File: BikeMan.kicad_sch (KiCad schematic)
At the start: 18 parts, among them J1 USB_A_stacked, J11 ExpansionSlotA, J12 ExpansionSlotB, J13 ExpansionSlotC, J14 CAN_{OUT}, J2 USB_A_stacked, J3 CAN_{IN}, J4 Barrel_Jack, J5 GPIO Outputs, J6 GPIO Inputs, J7 CAN / Power / GND

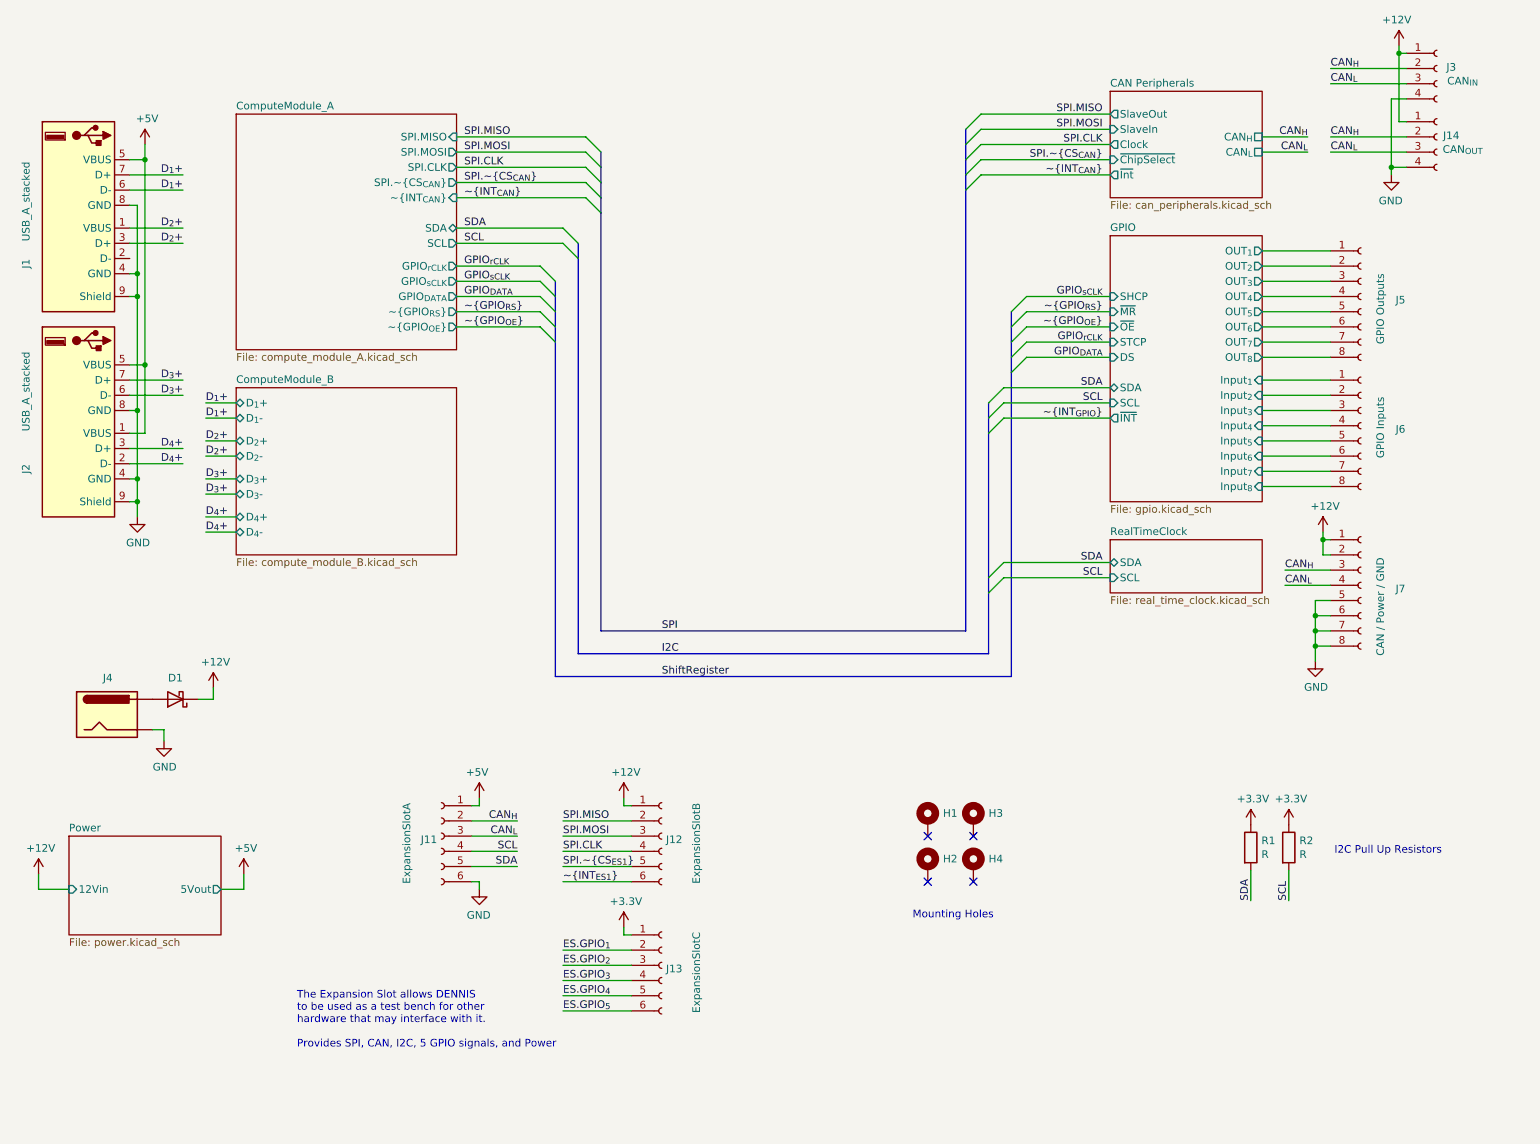
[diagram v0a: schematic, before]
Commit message: more layout: power supply and gpio
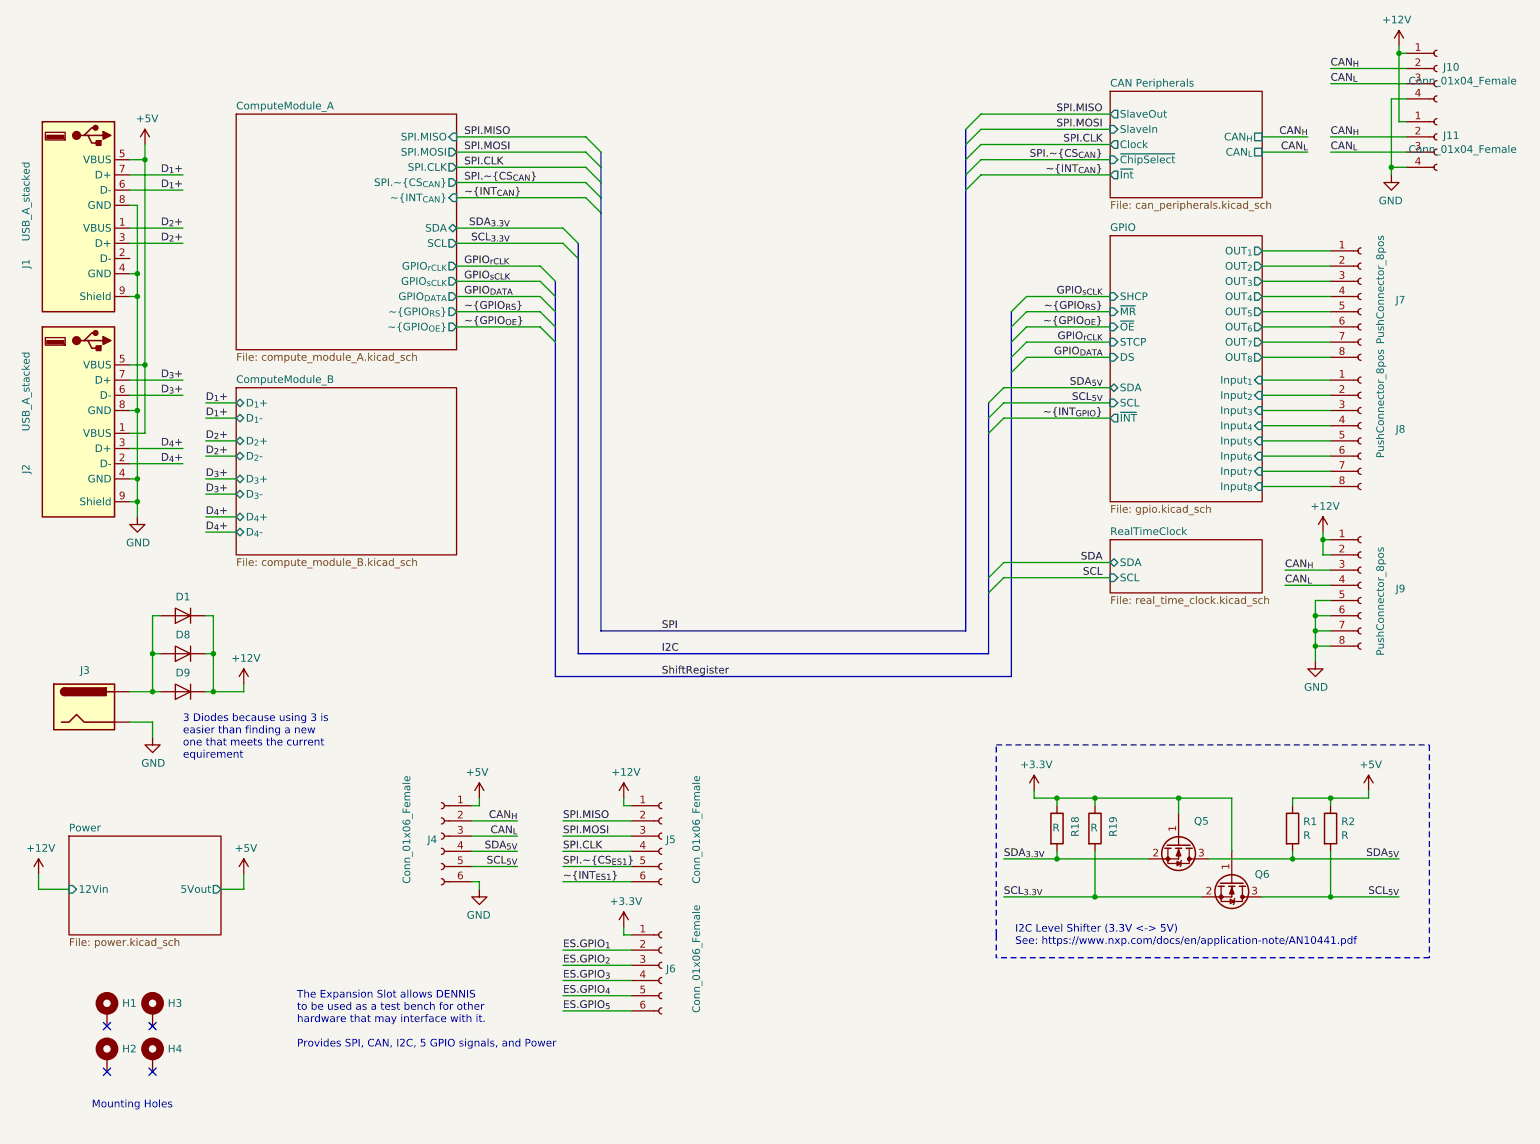
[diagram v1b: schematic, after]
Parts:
- removed D1: D_Schottky, symbol Device:D_Schottky
- added D1, D8, D9: Diode, Diode_SMD:D_SOD-123F, symbol symbols:Diode
- added Q5, Q6: DMN62D0U-7, Package_TO_SOT_SMD:SOT-23, symbol symbols:DMN62D0U-7
- added R18, R19: R, Resistor_SMD:R_0805_2012Metric, symbol Device:R
- J10: renamed from J3; value CAN_{IN} -> Conn_01x04_Female
- J11: renamed from J14; value CAN_{OUT} -> Conn_01x04_Female
- J4: renamed from J11; value ExpansionSlotA -> Conn_01x06_Female
- J5: renamed from J12; value ExpansionSlotB -> Conn_01x06_Female
- J6: renamed from J13; value ExpansionSlotC -> Conn_01x06_Female
- J7: renamed from J5; value GPIO Outputs -> PushConnector_8pos
- J8: renamed from J6; value GPIO Inputs -> PushConnector_8pos
- J9: renamed from J7; value CAN / Power / GND -> PushConnector_8pos
- renumbered J4 to J3
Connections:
- net +12V: now also D1.1 (K), D8.1 (K), D9.1 (K)
- net +3V3: now also Q5.1 (G), Q6.1 (G), R18.1, R19.1; no longer R1.1, R2.1
- net +5V: now also R1.1, R2.1
- net SCL: no longer J4.4 (Pin_4), R2.2
- net SDA: no longer J4.5 (Pin_5), R1.2
- net at J3.1: now also D1.2 (A), D8.2 (A), D9.2 (A)
- new net SCL_{3.3V}: Q6.2 (S), R19.2
- new net SCL_{5V}: J4.5 (Pin_5), Q6.3 (D), R2.2
- new net SDA_{3.3V}: Q5.2 (S), R18.2
- new net SDA_{5V}: J4.4 (Pin_4), Q5.3 (D), R1.2
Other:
- note added: "3 Diodes because using 3 is easier than finding a new one that meets the current equirement"
- note added: "I2C Level Shifter (3.3V <-> 5V) See: https://www.nxp.com/docs/en/application-note/AN10441.pdf"
- note removed: "I2C Pull Up Resistors"
- moved on the sheet: H1, H2, H3, H4, J3, R1, R2

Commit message: Routing for HDMI, Ethernet, SD Card, CAN
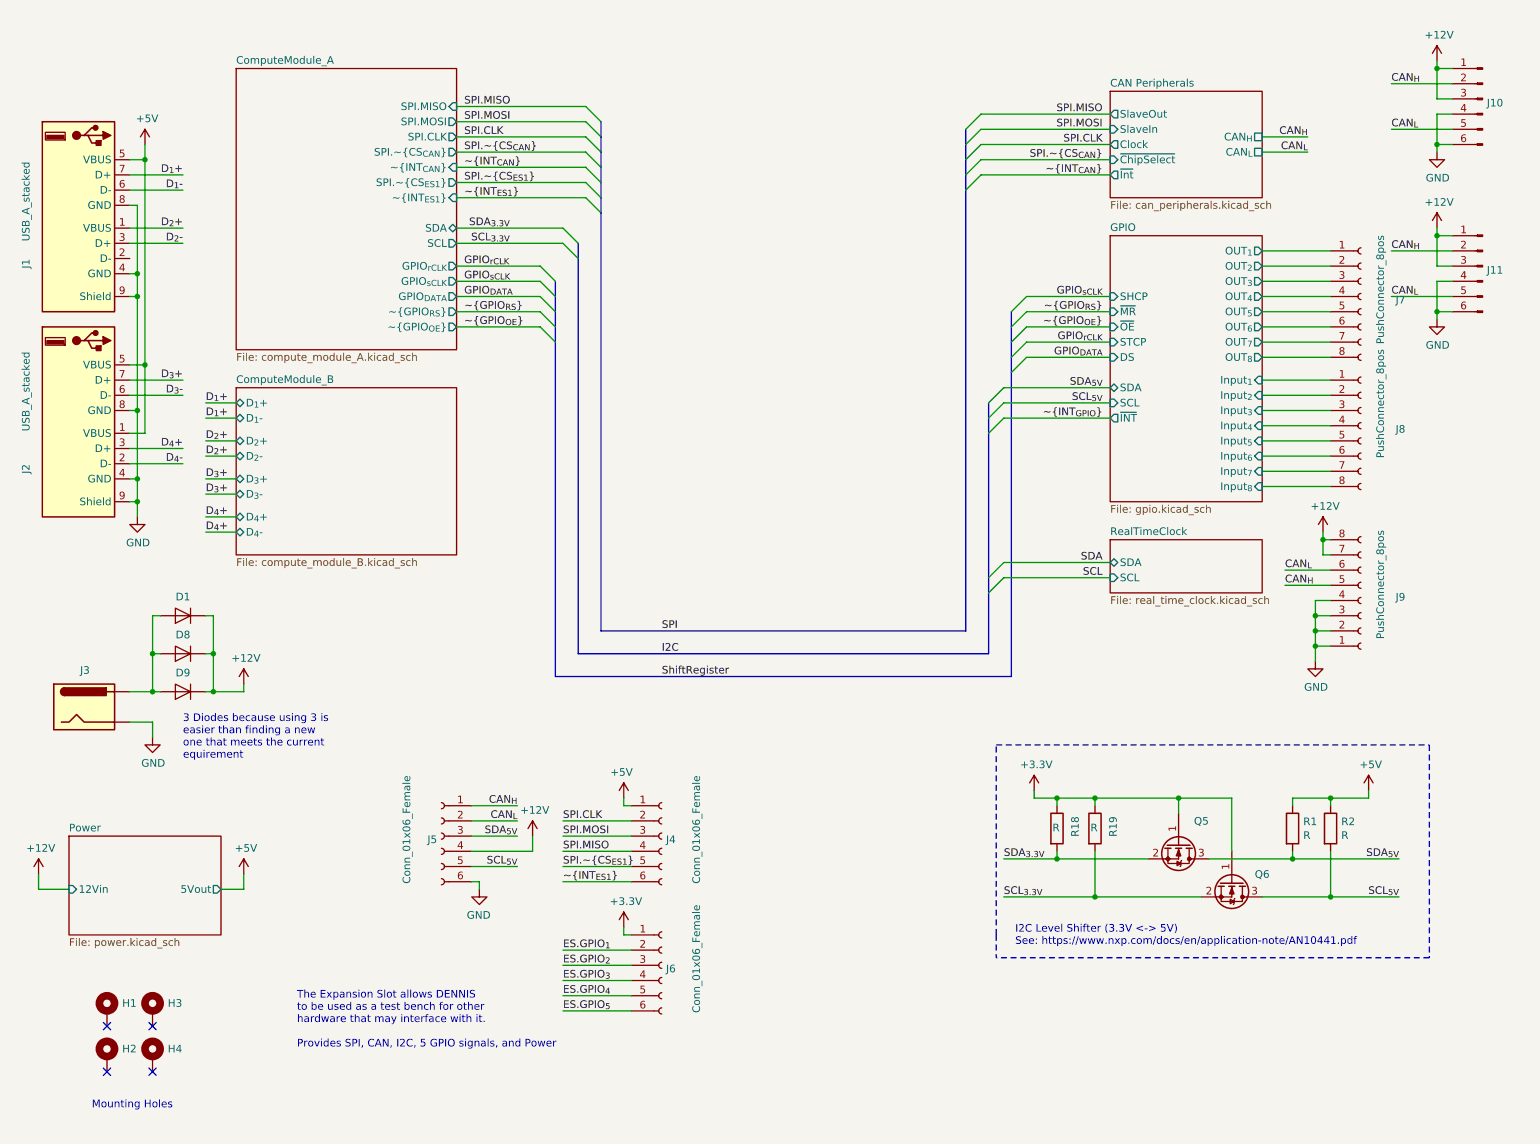
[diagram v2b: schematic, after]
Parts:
- removed J10, J11: Conn_01x04_Female, Connector_Molex:Molex_Micro-Fit_3.0_43045-0412_2x02_P3.00mm_Vertical, symbol Connector:Conn_01x04_Female
- added J10, J11: Conn_01x06_Male, Connector_PinSocket_2.54mm:PinSocket_2x03_P2.54mm_Vertical, symbol Connector:Conn_01x06_Male
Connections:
- net +12V: now also J5.4 (Pin_4), J9.7 (Pin_7), J9.8 (Pin_8), J10.1 (Pin_1), J10.3 (Pin_3), J11.1 (Pin_1), J11.3 (Pin_3); no longer J5.1 (Pin_1), J9.1 (Pin_1), J9.2 (Pin_2)
- net CAN_{H}: now also J5.1 (Pin_1), J9.5 (Pin_5), J10.2 (Pin_2), J11.2 (Pin_2); no longer J4.2 (Pin_2), J9.3 (Pin_3)
- net CAN_{L}: now also J5.2 (Pin_2), J9.6 (Pin_6), J10.5 (Pin_5), J11.5 (Pin_5); no longer J4.3 (Pin_3), J9.4 (Pin_4)
- net D_{1}+: no longer J1.6 (D-)
- net D_{2}+: no longer J1.3 (D+)
- net D_{3}+: no longer J2.6 (D-)
- net D_{4}+: no longer J2.2 (D-)
- net GND: now also J5.6 (Pin_6), J9.1 (Pin_1), J9.2 (Pin_2), J9.3 (Pin_3), J9.4 (Pin_4), J10.4 (Pin_4), J10.6 (Pin_6), J11.4 (Pin_4), J11.6 (Pin_6); no longer J4.6 (Pin_6), J9.5 (Pin_5), J9.6 (Pin_6), J9.7 (Pin_7), J9.8 (Pin_8)
- net SCL_{5V}: now also J5.5 (Pin_5); no longer J4.5 (Pin_5)
- net SDA_{5V}: now also J5.3 (Pin_3); no longer J4.4 (Pin_4)
- net SPI.CLK: now also J4.2 (Pin_2); no longer J5.4 (Pin_4)
- net SPI.MISO: now also J4.4 (Pin_4); no longer J5.2 (Pin_2)
- net SPI.MOSI: now also J4.3 (Pin_3); no longer J5.3 (Pin_3)
- net SPI.~CS_{ES1}: now also J4.5 (Pin_5); no longer J5.5 (Pin_5)
- net ~INT_{ES1}: now also J4.6 (Pin_6); no longer J5.6 (Pin_6)
- new net D_{1}-: J1.6 (D-)
- new net D_{2}-: J1.3 (D+)
- new net D_{3}-: J2.6 (D-)
- new net D_{4}-: J2.2 (D-)
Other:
- sheet ComputeModule_A ports: added SPI.~CS_{ES1}, ~INT_{ES1}; removed none
- moved on the sheet: J4, J5

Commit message: Finished trace routing
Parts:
- renumbered D8 to D2, D9 to D3, J5 to J4, J4 to J5, Q5 to Q1, Q6 to Q2, R18 to R1, R19 to R2, R1 to R3, R2 to R4
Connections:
- net +5V: no longer J1.5 (VBUS), J2.1 (VBUS), J2.5 (VBUS)
- net D_{1}+: now also J2.7 (D+); no longer J1.7 (D+)
- net D_{1}-: now also J2.6 (D-); no longer J1.6 (D-)
- net D_{2}+: now also J2.3 (D+); no longer J1.1 (VBUS)
- net D_{2}-: now also J2.2 (D-); no longer J1.3 (D+)
- net D_{3}+: now also J1.3 (D+); no longer J2.7 (D+)
- net D_{3}-: now also J1.2 (D-); no longer J2.6 (D-)
- net D_{4}+: now also J1.7 (D+); no longer J2.3 (D+)
- net D_{4}-: now also J1.6 (D-); no longer J2.2 (D-)
- net ES.GPIO_{1}: now also J6.4 (Pin_4); no longer J6.2 (Pin_2)
- net ES.GPIO_{2}: now also J6.2 (Pin_2); no longer J6.3 (Pin_3)
- net ES.GPIO_{3}: now also J6.3 (Pin_3); no longer J6.4 (Pin_4)
- net PWR_IN: now reaches D1.2 (A), D2.2 (A), D3.2 (A), J3.1
- new net PWR_{1}: J2.5 (VBUS)
- new net PWR_{2}: J2.1 (VBUS)
- new net PWR_{3}: J1.5 (VBUS)
- new net PWR_{4}: J1.1 (VBUS)
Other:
- sheet RealTimeClock renamed I2C extras
- sheet ComputeModule_A ports: added ES.GPIO_{1}, ES.GPIO_{2}, ES.GPIO_{3}, ES.GPIO_{4}, ES.GPIO_{5}; removed none
- sheet ComputeModule_B ports: added PWR_{1}, PWR_{2}, PWR_{3}, PWR_{4}; removed none
- sheet I2C extras ports: added SCL_{3.3V}, SCL_{5V}, SDA_{3.3V}, SDA_{5V}; removed SCL, SDA
